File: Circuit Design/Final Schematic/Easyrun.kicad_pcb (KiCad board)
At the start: 2 copper layers, 100 x 93.1 mm, 75 parts, among them U1 ESP32-WROOM-32

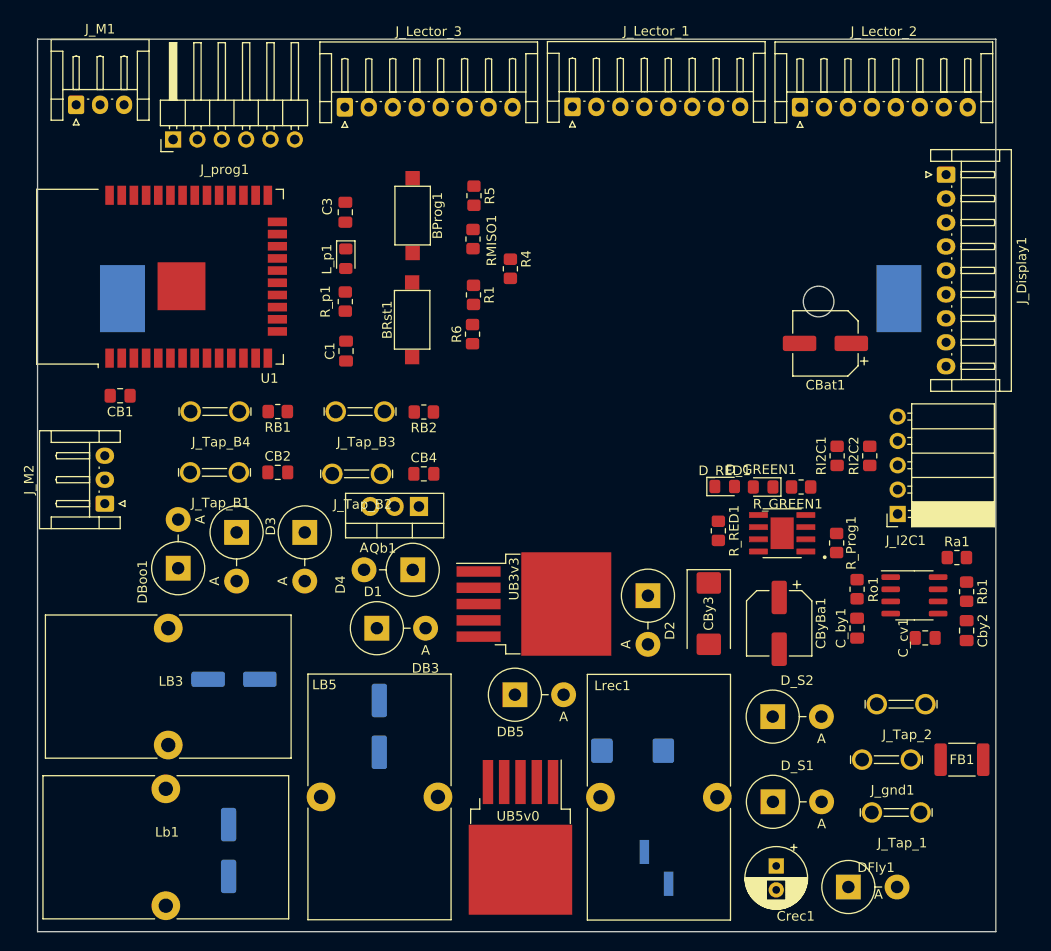
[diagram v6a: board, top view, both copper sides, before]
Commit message: Mounting holes
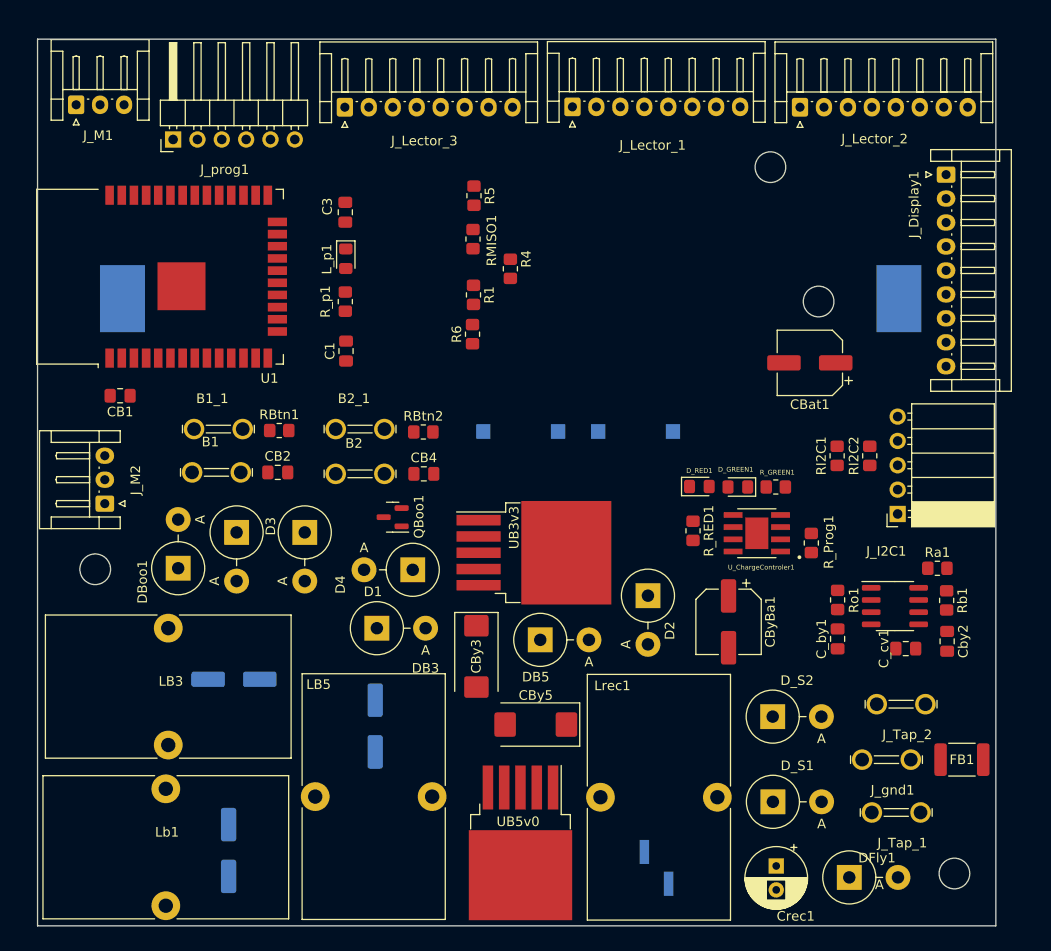
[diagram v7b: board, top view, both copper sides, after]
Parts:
- removed J_Tap_B1, J_Tap_B2, J_Tap_B3, J_Tap_B4: 62409-1, 62409-1_Connector_Faston:TE_62409-1
- removed Qb1: IRF740, Package_TO_SOT_THT:TO-220-3_Vertical
- removed RB2: 10K, Resistor_SMD:R_0805_2012Metric_Pad1.20x1.40mm_HandSolder
- removed the Rb1 at (168.9, 98.0)
- added B1: 62409-1, 62409-1_Connector_Faston:TE_62409-1, F.Cu at (90.6, 85.6)
- added B1_1: 62409-1, 62409-1_Connector_Faston:TE_62409-1, F.Cu at (90.8, 81.1)
- added B2: 62409-1, 62409-1_Connector_Faston:TE_62409-1, F.Cu at (105.6, 85.8)
- added B2_1: 62409-1, 62409-1_Connector_Faston:TE_62409-1, F.Cu at (105.6, 81.1)
- added QBoo1: SI2302, Package_TO_SOT_SMD:SOT-23, F.Cu at (109.0, 90.3)
- added RBtn1: 10K, Resistor_SMD:R_0805_2012Metric_Pad1.20x1.40mm_HandSolder, F.Cu at (97.2, 81.2)
- added RBtn2: 10K, Resistor_SMD:R_0805_2012Metric_Pad1.20x1.40mm_HandSolder, F.Cu at (112.2, 81.4)
- added REF**: MountingHole_3.2mm_M3_ISO14580, MountingHole:MountingHole_3.2mm_M3_ISO14580, F.Cu at (167.6, 127.5)
- added REF**: MountingHole_3.2mm_M3_ISO14580, MountingHole:MountingHole_3.2mm_M3_ISO14580, F.Cu at (148.4, 53.7)
- added REF**: MountingHole_3.2mm_M3_ISO14580, MountingHole:MountingHole_3.2mm_M3_ISO14580, F.Cu at (78.0, 95.7)
- BProg1, BRst1: moved to B.Cu
- CBy5: moved to F.Cu
- Rb1: renamed from RB1; value 10K -> 100
- moved Rb1 72.5 mm to (166.8, 99.0), turned to -90 degrees
- moved BProg1 32.4 mm to (134.4, 81.3), turned to 0 degrees
- moved CBy3 24.7 mm to (117.8, 104.8)
- moved BRst1 16.3 mm to (122.4, 81.3), turned to 180 degrees
- moved CBy5 10.5 mm to (124.0, 111.9), turned to 180 degrees
- moved DB5 6.31 mm to (124.4, 103.1)
- moved UB3v3 5.36 mm to (123.8, 94.0)
- moved CByBa1 5.29 mm to (144.1, 101.2)
- moved D_GREEN1 2.64 mm to (145.0, 87.1)
- moved R_GREEN1 2.64 mm to (149.0, 87.1)
- moved R_RED1 2.64 mm to (140.4, 91.7)
- moved D_RED1 2.64 mm to (141.0, 87.1)
- moved R_Prog1 2.64 mm to (152.7, 93.0)
- moved U_ChargeControler1 2.64 mm to (147.0, 91.9)
- moved CBat1 2.60 mm to (152.6, 74.2)
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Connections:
- Rb1 pad 1: GND -> Net-(Ra1-Pad2)
- Rb1 pad 2: /Butt_No_D -> /PowerModule/Boost_batt/TT
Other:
- board size 100 x 93.1 mm -> 100 x 92.5 mm

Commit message: Cambio orden pines lectores y display
Se cambiaron para facilitar el ruteo.
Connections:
- U1 pad 23: /CS_Display -> /D/C
- U1 pad 24: /CS_Lector3 -> /CS_Lector2
- U1 pad 36: /CS_Lector2 -> /CS_Lector3
- U1 pad 6: /Rst_D -> /CS_Display
- U1 pad 7: /D/C -> /Rst_D
